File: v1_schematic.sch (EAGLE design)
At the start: 212 parts, among them IC1 PCA82C250, IC2 FT232RL, IC3 SP3223EBP, IC4 MAX481CPA, IC5 LM2576T, Q1 25MHz, Q2 32.768kHz, Q3 2N2222A, T1 ST02-3.5MM, T3 2N2222, T4 2N2222, T5 2N2222, T6 2N2222, T7 2N2222, U1 ON_SEMICONDUCTOR_NCP1117ST33T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, U2 ON_SEMICONDUCTOR_NCP1117ST50T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, X1 MINI-USB-32005-201, X10 PC817SW, X11 PC817SW, X12 PC817SW, X13 PC817SW, X14 PC817SW, X15 PC817SW, X16 PC817SW, X17 PC817SW, X18 PC817SW, X19 PC817SW, X20 PC817SW, X21 PC817SW, X22 PC817SW, X23 PC817SW, X24 PC817SW, X6 SDBMF, X7 5566-8, X8 5566-8, X9 PC817SW

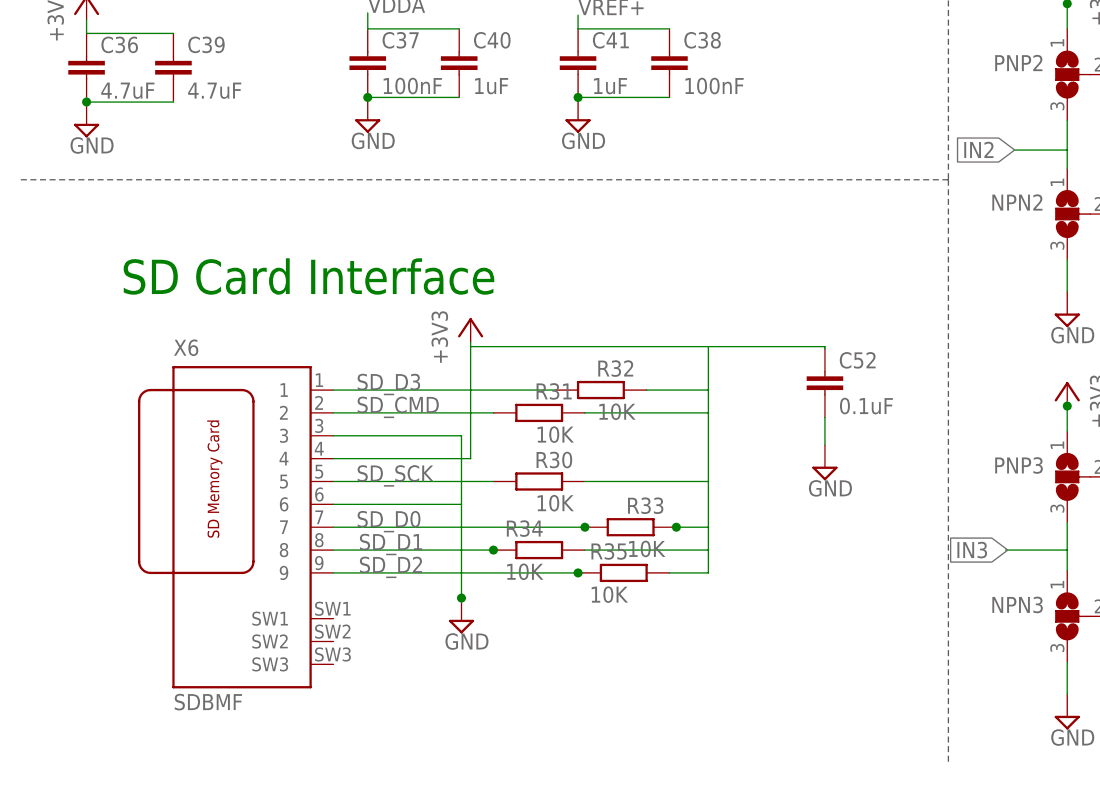
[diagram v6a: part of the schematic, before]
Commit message: SD Card Interface
- Changed interface to T-Flash Push-Out Micro SD Card Reader 14.75mm x 14.5mm SMD with external pins (smaller footprint)
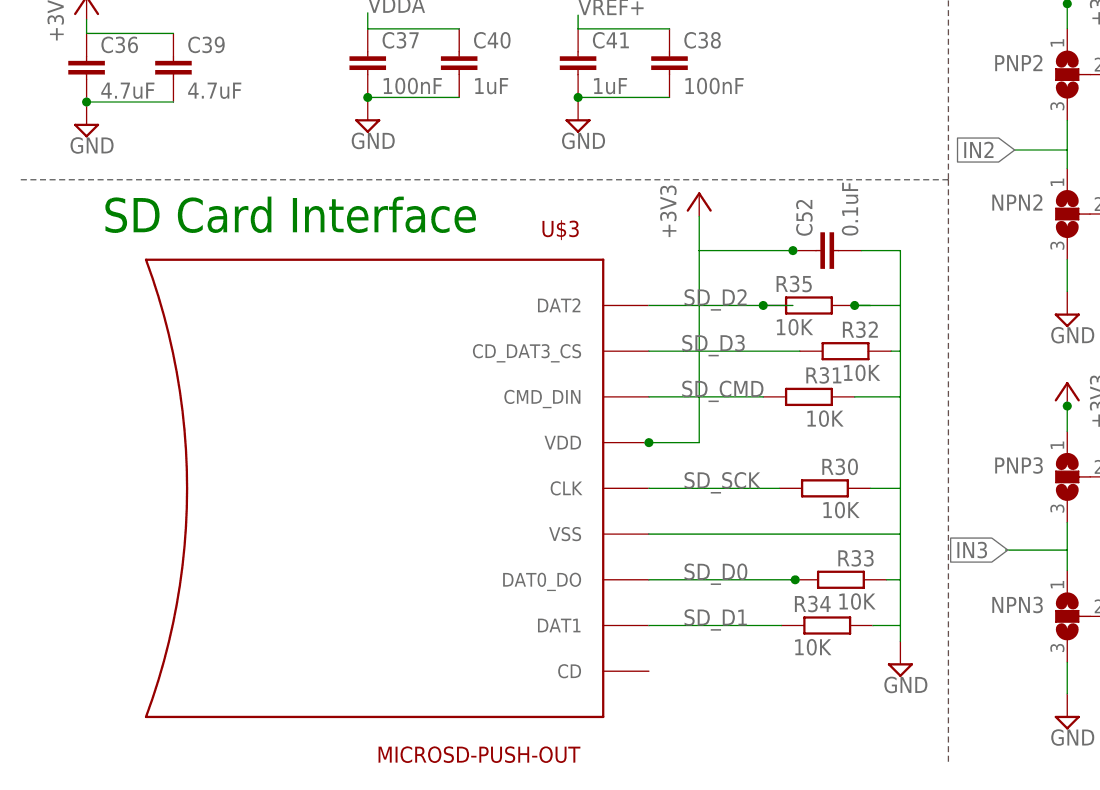
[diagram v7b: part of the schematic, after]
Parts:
- removed X6: SDBMF, farnell:SDBMF
- added U$3: MICROSD-PUSH-OUT, microsd:MICROSD-PUSH-OUT
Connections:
- net +3V3: now also U$3.VDD; no longer R30.1, R31.1, R32.1, R33.1, R34.2, R35.2, X6.4
- net GND: now also R30.1, R31.1, R32.1, R33.1, R34.2, R35.2, U$3.VSS; no longer X6.3, X6.6
- net SD_CMD: now also U$3.CMD_DIN; no longer X6.2
- net SD_D0: now also U$3.DAT0_DO; no longer X6.7
- net SD_D1: now also U$3.DAT1; no longer X6.8
- net SD_D2: now also U$3.DAT2; no longer X6.9
- net SD_D3: now also U$3.CD_DAT3_CS; no longer X6.1
- net SD_SCK: now also U$3.CLK; no longer X6.5
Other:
- moved on the sheet: C52, R30, R31, R32, R33, R34, R35

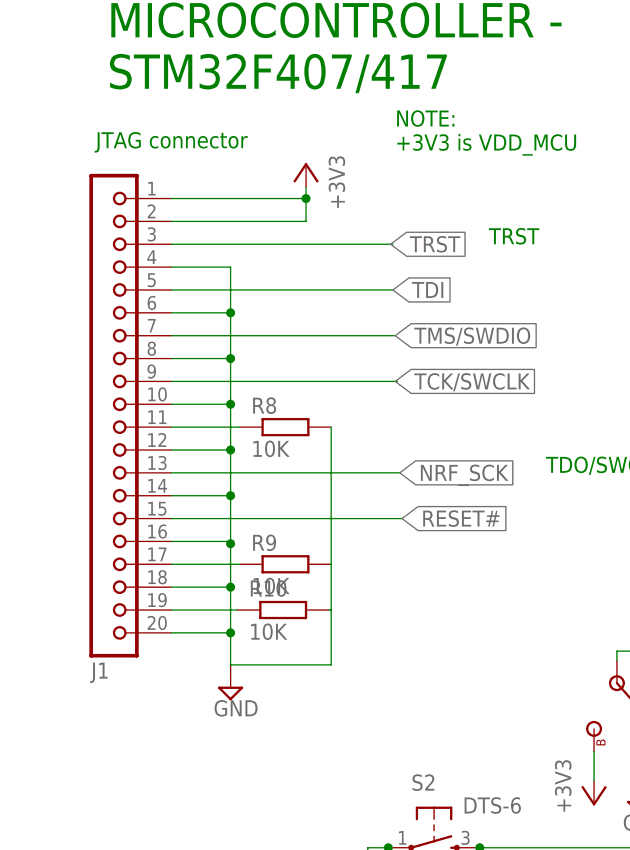
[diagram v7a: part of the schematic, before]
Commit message: JTAG connector
- Changed JTAG connector to dual row
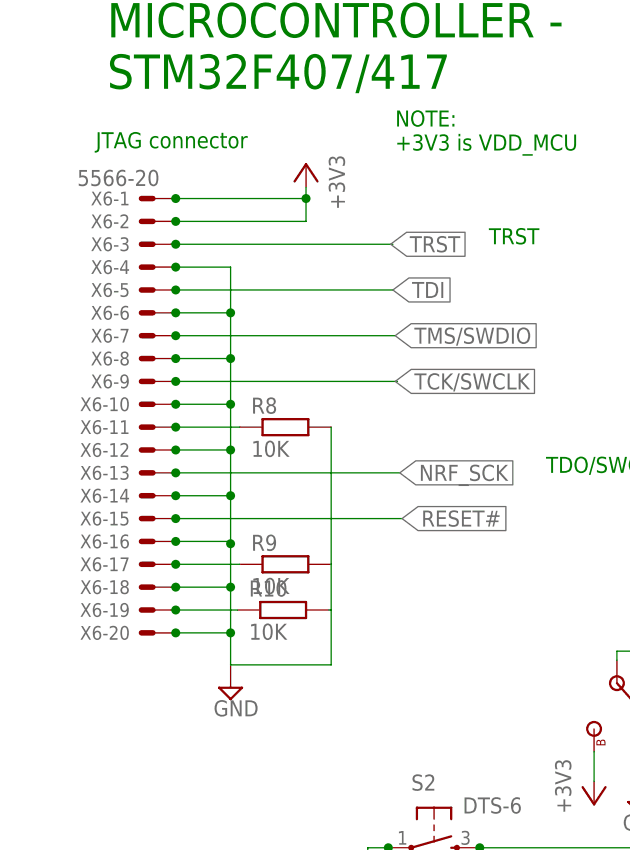
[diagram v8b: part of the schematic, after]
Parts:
- removed J1: (no value), con-lsta:JBK20
- added X6: 5566-20, con-molex:5566-20
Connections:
- net +3V3: now also X6-1.S, X6-2.S; no longer J1.1, J1.2
- net GND: now also X6-10.S, X6-12.S, X6-14.S, X6-16.S, X6-18.S, X6-20.S, X6-4.S, X6-6.S, X6-8.S; no longer J1.10, J1.12, J1.14, J1.16, J1.18, J1.20, J1.4, J1.6, J1.8
- net N$50: now also X6-11.S; no longer J1.11
- net N$53: now also X6-17.S; no longer J1.17
- net N$56: now also X6-19.S; no longer J1.19
- net NRF_SCK: now also X6-13.S; no longer J1.13
- net RESET#: now also X6-15.S; no longer J1.15
- net TCK/SWCLK: now also X6-9.S; no longer J1.9
- net TDI: now also X6-5.S; no longer J1.5
- net TMS/SWDIO: now also X6-7.S; no longer J1.7
- net TRST: now also X6-3.S; no longer J1.3
